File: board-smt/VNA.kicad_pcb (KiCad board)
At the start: 2 copper layers, 100 x 100 mm, 172 parts, among them J1 Conn_02x07_Odd_Even, J10 Conn_01x01, J11 Conn_01x01, J12 Conn_01x01, J13 Barrel_Jack, J14 Conn_01x01, J15 Conn_01x02, J16 Conn_01x01, J17 Conn_01x04, J18 Conn_01x01, J19 Conn_01x01, J2 Conn_Coaxial, J20 Conn_01x01, J21 Conn_01x01, J22 Conn_01x02, J24 USB_B, J3 Conn_01x01, J4 Conn_01x01, J5 Conn_01x01, J6 Conn_01x01, J7 Conn_01x01, J8 Conn_01x01, J9 Conn_Coaxial, Q3 S9018, SW1 SW_DPDT_x2, U1 SI5351A, U10 MT3608, U11 CN3052, U12 SI5351A, U2 LM339, U3 SA612, U4 SA612, U5 SA612, U6 LM358, U7 LM358, U8 AMS1117-3V3, U9 78M05_TO252, Y1 27 MHz

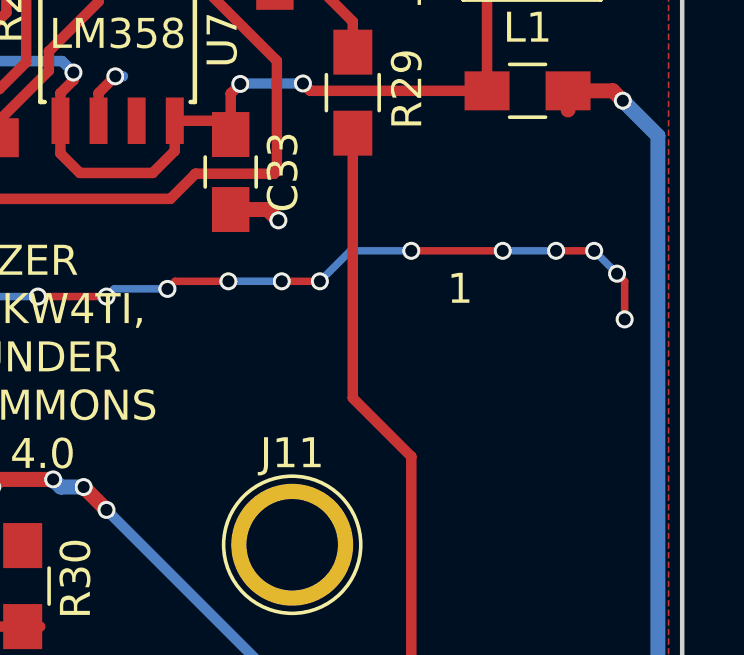
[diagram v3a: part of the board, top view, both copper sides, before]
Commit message: Added VNA-O-MIZER Logo
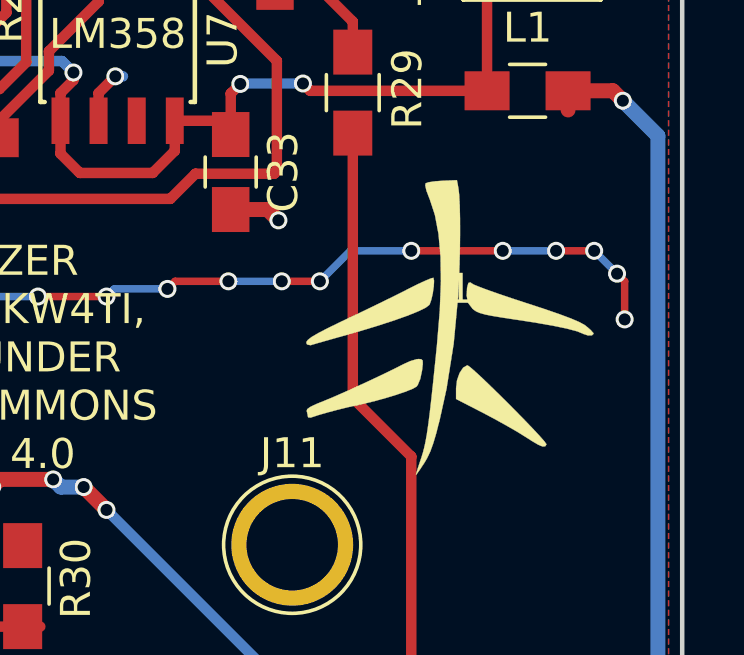
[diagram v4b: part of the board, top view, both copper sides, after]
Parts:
- added G***: LOGO, VNA:VNAOMizer, F.Cu at (142.2, 94.8)
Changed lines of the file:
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@@
     (tracks 2920)
     (zones 0)
-    (modules 172)
+    (modules 173)
     (nets 107)
   )
@@
     )
   )
+  (module VNA:VNAOMizer (layer F.Cu)
+    (at 142.25 94.75)
+    (fp_text reference G*** (at 0 0) (layer F.SilkS) hide
+      (effects (font (thickness 0.3)))
+    )
+    (fp_text value LOGO (at 0.75 0) (layer F.SilkS) hide
+      (effects (font (thickness 0.3)))
+    )
+    (fp_poly (pts (xy 0.293123 -4.621389) (xy 0.317894 -4.398101) (xy 0.334924 -4.059111) (xy 0.344295 -3.629613)
+      (xy 0.34609 -3.134799) (xy 0.340391 -2.599861) (xy 0.327282 -2.049993) (xy 0.306845 -1.510387)
+      (xy 0.281376 -1.040503) (xy 0.132851 0.549482) (xy -0.105598 2.051599) (xy -0.329137 3.068511)
+      (xy -0.44618 3.524507) (xy -0.548457 3.872163) (xy -0.646898 4.141893) (xy -0.752432 4.364109)
+      (xy -0.859182 4.543478) (xy -0.990915 4.742234) (xy -1.086976 4.877522) (xy -1.128467 4.922866)
+      (xy -1.128889 4.921308) (xy -1.107542 4.840305) (xy -1.050995 4.66136) (xy -0.970491 4.419781)
+      (xy -0.951308 4.363564) (xy -0.898844 4.199208) (xy -0.851171 4.020657) (xy -0.806283 3.813472)
+      (xy -0.76217 3.563215) (xy -0.716825 3.255448) (xy -0.668239 2.875732) (xy -0.614404 2.40963)
+      (xy -0.553313 1.842704) (xy -0.482956 1.160514) (xy -0.422889 0.564444) (xy -0.332038 -0.538475)
+      (xy -0.293424 -1.515472) (xy -0.307325 -2.371822) (xy -0.374021 -3.1128) (xy -0.49379 -3.743681)
+      (xy -0.666911 -4.269739) (xy -0.680017 -4.300431) (xy -0.776027 -4.552624) (xy -0.816049 -4.729629)
+      (xy -0.80382 -4.798291) (xy -0.705213 -4.833254) (xy -0.507852 -4.863601) (xy -0.254079 -4.882859)
+      (xy -0.248985 -4.883076) (xy 0.2416 -4.903612) (xy 0.293123 -4.621389)) (layer F.SilkS) (width 0.01))
+    (fp_poly (pts (xy 0.668263 1.317823) (xy 0.82314 1.450533) (xy 1.041855 1.651986) (xy 1.308286 1.906042)
+      (xy 1.606316 2.196557) (xy 1.919825 2.507389) (xy 2.232692 2.822398) (xy 2.5288 3.12544)
+      (xy 2.792028 3.400373) (xy 3.006256 3.631056) (xy 3.155366 3.801346) (xy 3.223238 3.895102)
+      (xy 3.225398 3.905751) (xy 3.182105 3.970047) (xy 3.099226 3.976528) (xy 2.956451 3.918004)
+      (xy 2.733471 3.787287) (xy 2.540815 3.663418) (xy 2.271595 3.49674) (xy 1.919779 3.292474)
+      (xy 1.529298 3.075503) (xy 1.144085 2.87071) (xy 1.112065 2.854184) (xy 0.211667 2.390755)
+      (xy 0.211667 2.035297) (xy 0.243772 1.767589) (xy 0.32785 1.526408) (xy 0.445544 1.34856)
+      (xy 0.578497 1.270853) (xy 0.593341 1.27) (xy 0.668263 1.317823)) (layer F.SilkS) (width 0.01))
+    (fp_poly (pts (xy -0.946216 1.065488) (xy -0.900925 1.10942) (xy -0.896299 1.223823) (xy -0.922406 1.442396)
+      (xy -0.924452 1.457488) (xy -0.981931 1.726207) (xy -1.064968 1.924752) (xy -1.10667 1.978735)
+      (xy -1.230238 2.049751) (xy -1.462247 2.143052) (xy -1.773553 2.249581) (xy -2.135011 2.360284)
+      (xy -2.517475 2.466105) (xy -2.891801 2.557989) (xy -3.139722 2.610395) (xy -3.407776 2.668996)
+      (xy -3.736706 2.750557) (xy -4.078508 2.84215) (xy -4.385181 2.930848) (xy -4.608723 3.003724)
+      (xy -4.630389 3.011827) (xy -4.715506 3.006539) (xy -4.727222 2.976652) (xy -4.750819 2.849293)
+      (xy -4.767361 2.799718) (xy -4.751137 2.730729) (xy -4.640454 2.649848) (xy -4.418805 2.54681)
+      (xy -4.255833 2.481694) (xy -3.959586 2.360263) (xy -3.572416 2.19175) (xy -3.129516 1.99238)
+      (xy -2.666076 1.778374) (xy -2.217289 1.565958) (xy -1.818347 1.371353) (xy -1.541823 1.23054)
+      (xy -1.318736 1.13034) (xy -1.1183 1.068245) (xy -1.042105 1.058333) (xy -0.946216 1.065488)) (layer F.SilkS) (width 0.01))
+    (fp_poly (pts (xy -0.542509 -1.64788) (xy -0.521421 -1.549341) (xy -0.530529 -1.363452) (xy -0.56247 -1.138882)
+      (xy -0.609884 -0.924303) (xy -0.665407 -0.768384) (xy -0.679048 -0.745207) (xy -0.798112 -0.65308)
+      (xy -1.042072 -0.532947) (xy -1.398515 -0.389323) (xy -1.855024 -0.226725) (xy -2.399185 -0.04967)
+      (xy -3.018582 0.137325) (xy -3.421944 0.252633) (xy -3.804445 0.360157) (xy -4.142102 0.455712)
+      (xy -4.410267 0.532274) (xy -4.584297 0.582817) (xy -4.636768 0.598905) (xy -4.747126 0.577683)
+      (xy -4.770388 0.551681) (xy -4.777941 0.491533) (xy -4.724056 0.417029) (xy -4.596658 0.320843)
+      (xy -4.38367 0.195646) (xy -4.073018 0.034112) (xy -3.652626 -0.171087) (xy -3.316111 -0.330735)
+      (xy -2.868776 -0.543522) (xy -2.396326 -0.771903) (xy -1.941683 -0.994892) (xy -1.54777 -1.191506)
+      (xy -1.367319 -1.283497) (xy -1.066596 -1.433976) (xy -0.812523 -1.552478) (xy -0.630213 -1.62791)
+      (xy -0.544776 -1.649177) (xy -0.542509 -1.64788)) (layer F.SilkS) (width 0.01))
+    (fp_poly (pts (xy 0.731539 -1.46223) (xy 0.818222 -1.415777) (xy 1.020676 -1.333993) (xy 1.319994 -1.223676)
+      (xy 1.69727 -1.091624) (xy 2.1336 -0.944634) (xy 2.54 -0.811992) (xy 3.1671 -0.606363)
+      (xy 3.667291 -0.433407) (xy 4.050033 -0.289514) (xy 4.324785 -0.171074) (xy 4.501006 -0.074478)
+      (xy 4.533195 -0.051462) (xy 4.689368 0.081748) (xy 4.784372 0.186969) (xy 4.797778 0.217595)
+      (xy 4.741426 0.270517) (xy 4.610175 0.272792) (xy 4.460733 0.22468) (xy 4.445 0.215962)
+      (xy 4.245346 0.135201) (xy 3.909109 0.045705) (xy 3.440487 -0.051644) (xy 2.843679 -0.155962)
+      (xy 2.222161 -0.251889) (xy 1.762746 -0.320933) (xy 1.421289 -0.377361) (xy 1.175812 -0.426708)
+      (xy 1.004335 -0.474508) (xy 0.884877 -0.526294) (xy 0.795458 -0.587601) (xy 0.758473 -0.620418)
+      (xy 0.608861 -0.816858) (xy 0.564488 -1.055794) (xy 0.564445 -1.065764) (xy 0.58005 -1.332126)
+      (xy 0.624665 -1.477904) (xy 0.694992 -1.495271) (xy 0.731539 -1.46223)) (layer F.SilkS) (width 0.01))
+  )
   (gr_text 1 (at 87.3 101.9) (layer F.SilkS)

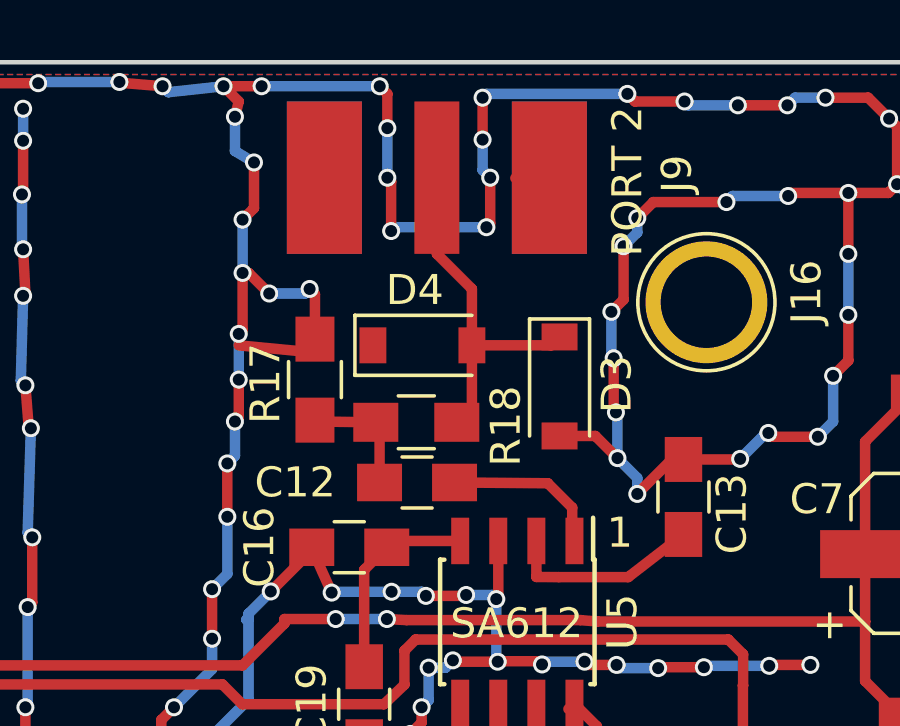
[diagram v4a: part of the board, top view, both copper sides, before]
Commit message: Tweaked the layout on port 2
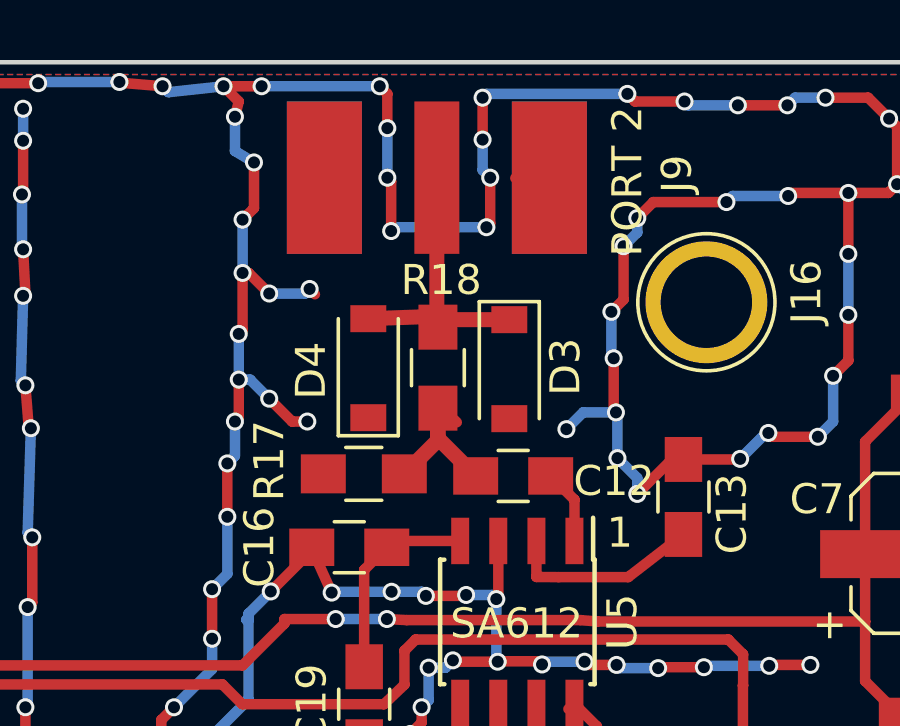
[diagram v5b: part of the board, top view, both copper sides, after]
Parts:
- moved R17 3.54 mm to (125.6, 63.7), turned to 180 degrees
- moved C12 3.21 mm to (130.6, 63.8)
- moved R18 1.96 mm to (128.1, 60.2), turned to 90 degrees
- moved D4 1.96 mm to (125.7, 60.2), turned to 90 degrees
- moved D3 1.77 mm to (130.4, 60.2)
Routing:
- net Net-(C12-Pad1): track 5.40 -> 2.60 mm
- net Net-(D3-Pad1): track 14.5 -> 12.0 mm
- net GND: track 1353.1 -> 1351.4 mm, vias 520 -> 523

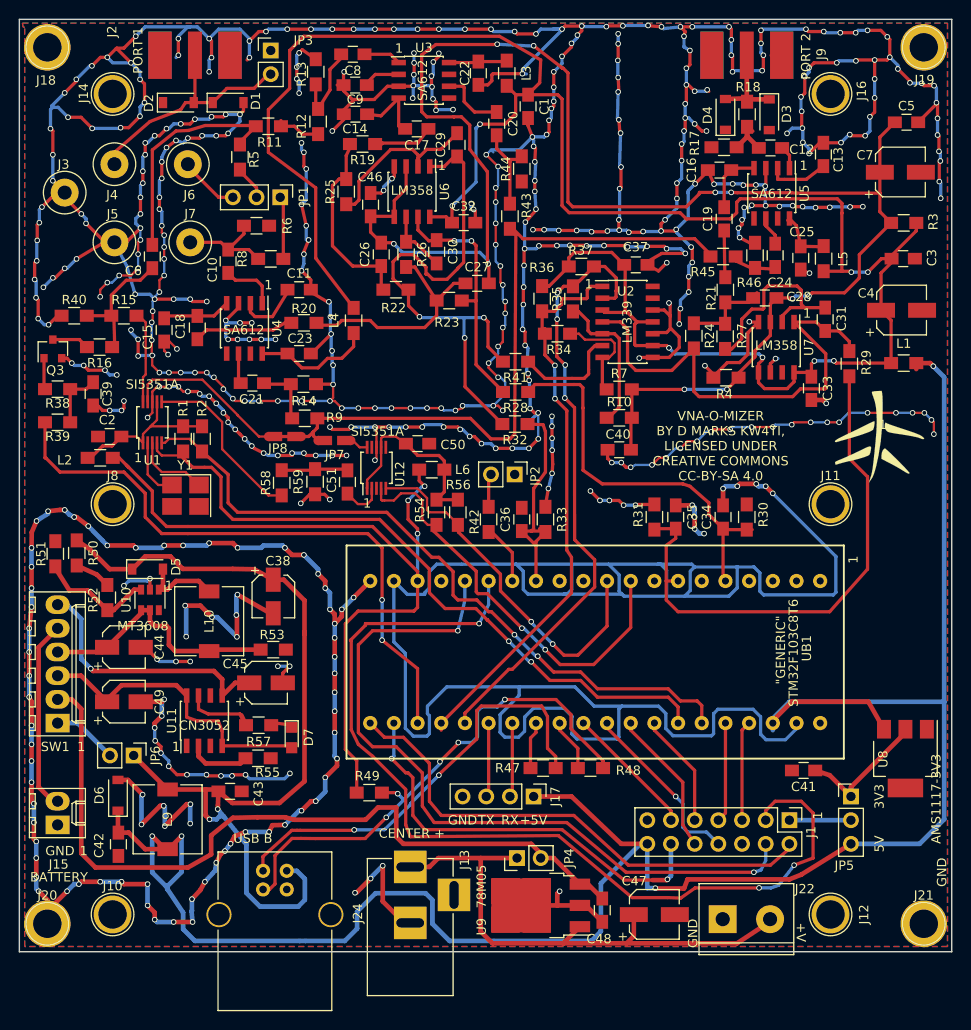
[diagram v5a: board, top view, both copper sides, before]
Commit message: Fixed crystal pinout, added heatsink pad to CN3052A
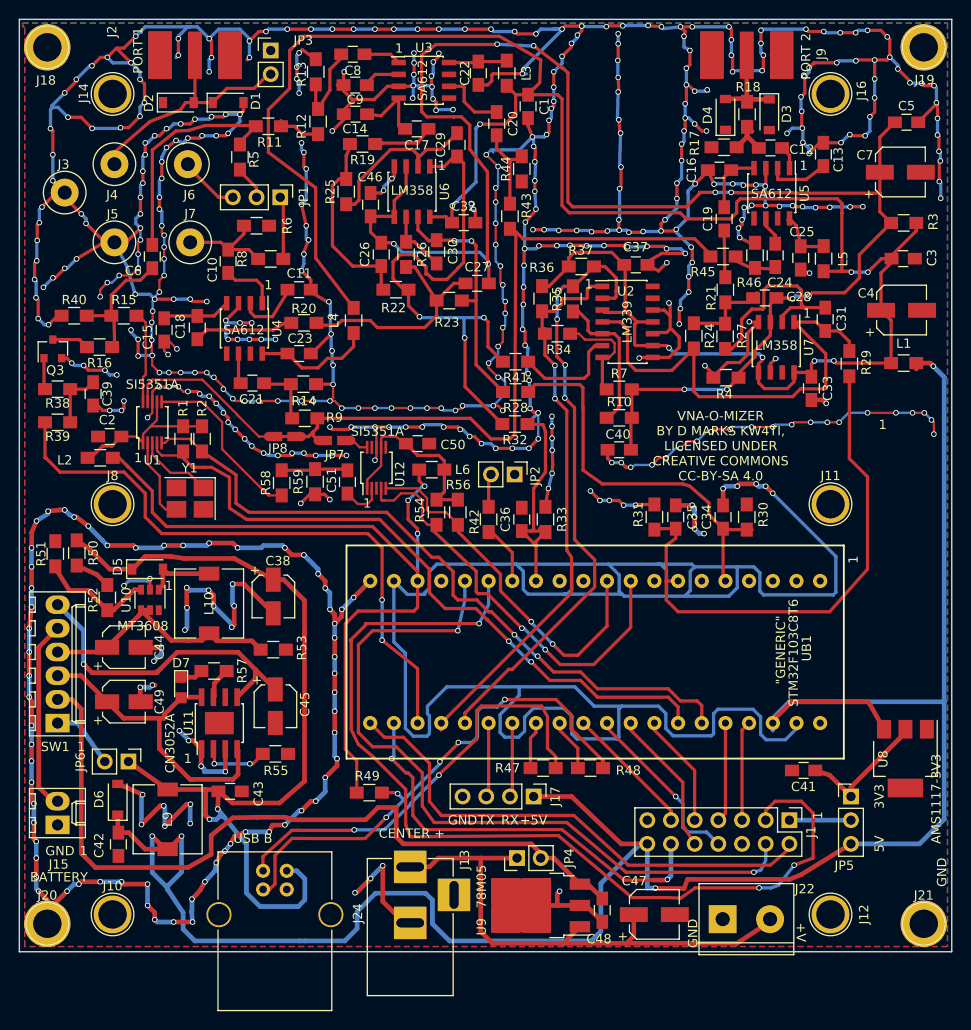
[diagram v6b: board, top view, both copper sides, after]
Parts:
- removed G***: LOGO, VNA:VNAOMizer
- R55: value 4k7 -> 10k
- U11: footprint Housings_SOIC:SOIC-8_3.9x4.9mm_Pitch1.27mm -> Housings_SOIC:TI_SO-PowerPAD-8
- moved D7 13.0 mm to (67.3, 121.7)
- moved R57 7.53 mm to (70.9, 119.9), turned to 0 degrees
- moved C45 2.70 mm to (77.5, 123.7), turned to 270 degrees
- moved R55 1.91 mm to (77.5, 128.8)
- moved L10 1.90 mm to (70.3, 112.7)
- moved U11 1.62 mm to (71.5, 125.5)
- moved JP6 0.86 mm to (61.7, 129.6)
- moved Y1 0.57 mm to (68.3, 101.4)
- moved D6 0.43 mm to (60.5, 133.7)
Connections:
- Y1 pad 2: Net-(U1-Pad2) -> (no net)
- Y1 pad 3: (no net) -> Net-(U1-Pad2)
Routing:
- net GND: track 1351.4 -> 1339.9 mm, vias 523 -> 516
- net Net-(C45-Pad1): track 28.7 -> 36.2 mm
- net Net-(R57-Pad2): track 8.59 -> 3.40 mm
- net Net-(U1-Pad2): track 6.47 -> 9.10 mm
- net Net-(C49-Pad1): track 33.5 -> 35.4 mm
- net Net-(C44-Pad1): track 27.5 -> 28.8 mm
- net Net-(D5-Pad2): track 8.64 -> 7.53 mm
- net Net-(R55-Pad2): track 7.35 -> 7.26 mm, vias 0 -> 2
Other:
- board text added: "CN3052A"
- board text removed: "CN3052"

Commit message: Fixed a few more outstanding issues
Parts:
- moved R10 0.76 mm to (115.1, 93.0)
- moved C40 0.74 mm to (115.1, 96.0)
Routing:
- net GND: track 1339.9 -> 1359.4 mm, vias 516 -> 529

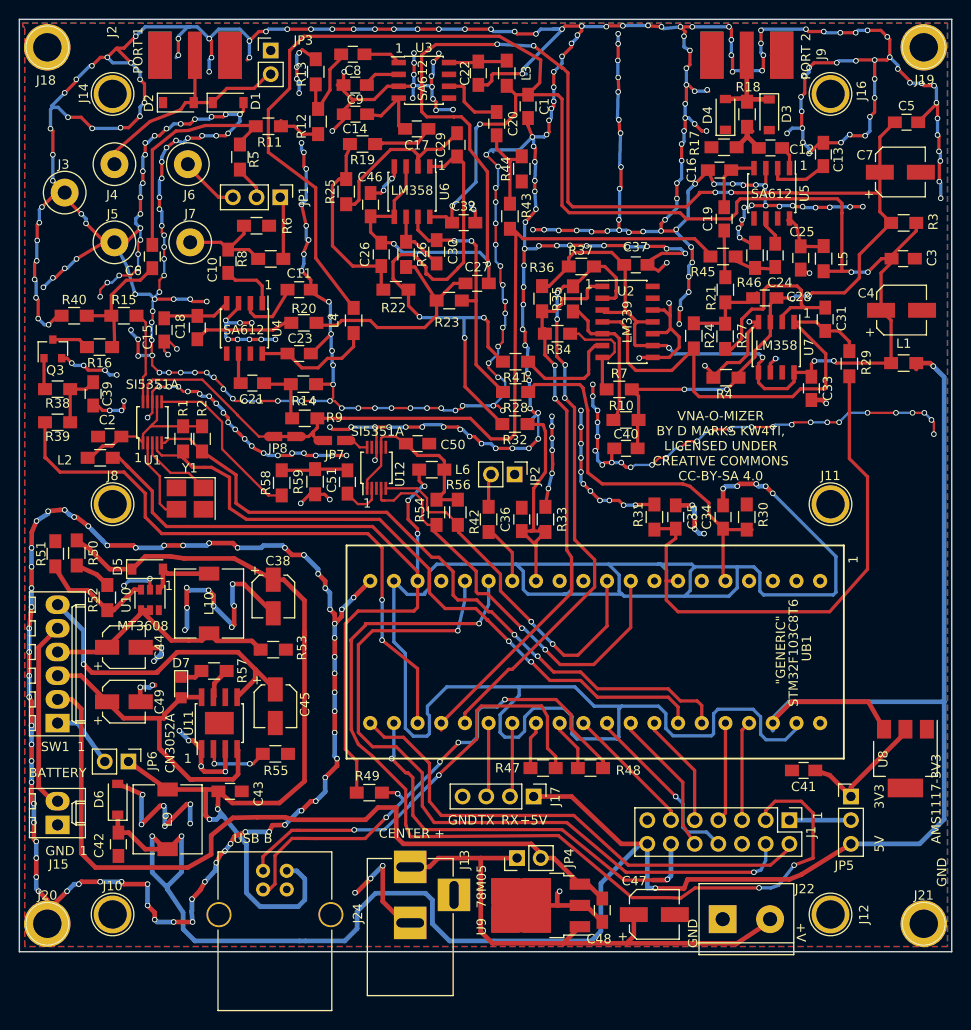
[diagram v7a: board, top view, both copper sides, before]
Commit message: Changed Schottky diode to SS14 and 1N4148 to BAV99
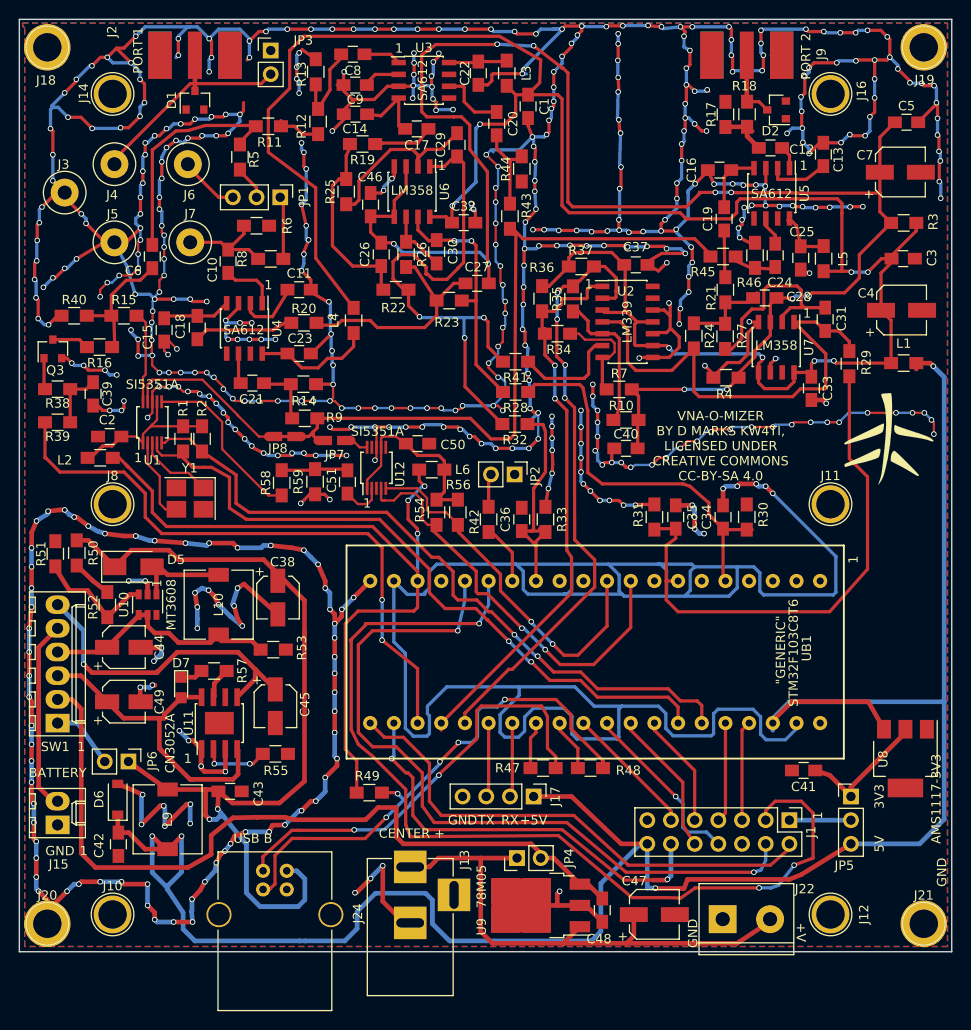
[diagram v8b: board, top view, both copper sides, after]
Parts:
- removed D3, D4: 1N4148, Diodes_SMD:D_SOD-123
- added G***: LOGO, VNA:VNAOMizer, F.Cu at (143.3, 95.0)
- D1, D2: value 1N4148 -> BAV99; footprint Diodes_SMD:D_SOD-123 -> TO_SOT_Packages_SMD:SOT-23
- D5: value D_Schottky -> SS14; footprint Diodes_SMD:D_SOD-123 -> Diodes_SMD:D_SMA
- L10: value L_Small -> 10 uH
- moved D2 64.2 mm to (131.2, 59.7), turned to 180 degrees
- moved D1 3.57 mm to (68.8, 58.7), turned to 90 degrees
- moved R17 3.53 mm to (125.7, 60.2), turned to 90 degrees
- moved D5 1.55 mm to (62.2, 108.7)
- moved L10 1.03 mm to (71.4, 112.8)
- moved R52 0.76 mm to (59.4, 112.8)
- moved U10 0.57 mm to (63.8, 112.8)
- moved C38 0.51 mm to (77.7, 112.0)
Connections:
- D1 pad 1: Net-(D1-Pad1) -> GND
- D2 pad 2: Net-(D1-Pad1) -> GND
- J2 pad 1: Net-(D1-Pad1) -> Net-(D1-Pad3)
- J4 pad 1: Net-(D1-Pad1) -> Net-(D1-Pad3)
- J9 pad 1: Net-(D3-Pad1) -> Net-(D2-Pad3)
- JP3 pad 2: Net-(D1-Pad1) -> Net-(D1-Pad3)
- R18 pad 2: Net-(D3-Pad1) -> Net-(D2-Pad3)
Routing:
- net Net-(D1-Pad1): track 27.9 -> 0.00 mm
- net Net-(D1-Pad3): track 0.00 -> 27.2 mm
- net Net-(D3-Pad1): track 12.0 -> 0.00 mm
- net Net-(D2-Pad3): track 0.00 -> 10.5 mm
- net GND: track 1359.4 -> 1355.9 mm
- net Net-(D5-Pad2): track 7.53 -> 10.7 mm
- net Net-(C44-Pad1): track 28.8 -> 27.4 mm
- net POWFILT: track 98.0 -> 99.4 mm
